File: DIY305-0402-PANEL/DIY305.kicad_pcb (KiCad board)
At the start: 2 copper layers, 49.8 x 26.6 mm, 152 parts, among them J1 Conn_01x07, J2 Conn_01x07, J3 Conn_01x07, J4 Conn_01x07, J5 Conn_01x07, J6 Conn_01x07, J7 Conn_01x07, J8 Conn_01x07

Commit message: Added pannel
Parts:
- removed D100, D101, D102, D103, D104, D105, D106, D107, D108, D109, D110, D111, D112, D113, D114, D115, D116, D117, D118, D119, D120, D121, D122, D123, D124, D125, D126, D127, D128, D129, D130, D131, D132, D133, D134, D135, D136, D137, D138, D139, D140, D141, D142, D143, D144, D37, D38, D39, D40, D41, D42, D43, D44, D45, D46, D47, D48, D49, D50, D51, D52, D53, D54, D55, D56, D57, D58, D59, D60, D61, D62, D63, D64, D65, D66, D67, D68, D69, D70, D71, D72, D73, D74, D75, D76, D77, D78, D79, D80, D81, D82, D83, D84, D85, D86, D87, D88, D89, D90, D91, D92, D93, D94, D95, D96, D97, D98, D99: LED, LED_SMD:LED_0402_1005Metric
- removed J3, J4, J5, J6, J7, J8: Conn_01x07, Connector_PinHeader_2.54mm:PinHeader_1x07_P2.54mm_Vertical
- moved J1 14.8 mm to (28.7, 21.6)
- moved D1 9.41 mm to (22.4, 23.2)
- moved D10 9.41 mm to (23.6, 27.2)
- moved D11 9.41 mm to (23.6, 29.2)
- moved D12 9.41 mm to (23.6, 31.2)
- moved D13 9.41 mm to (23.6, 33.2)
- moved D14 9.41 mm to (23.6, 35.2)
- moved D15 9.41 mm to (24.9, 23.2)
- moved D16 9.41 mm to (24.9, 25.2)
- moved D17 9.41 mm to (24.9, 27.2)
- moved D18 9.41 mm to (24.9, 29.2)
- moved D19 9.41 mm to (24.9, 31.2)
- moved D2 9.41 mm to (22.4, 25.2)
- moved D20 9.41 mm to (24.9, 33.2)
- moved D21 9.41 mm to (24.9, 35.2)
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- renumbered D11 to D10, D12 to D11, D13 to D12, D14 to D13, D15 to D14, D16 to D15, D17 to D16, D18 to D17, D19 to D18, D20 to D19, D21 to D20, D22 to D21, D23 to D22, D24 to D23, D25 to D24, D26 to D25, D27 to D26, D28 to D27, D29 to D28, D30 to D29, D31 to D30, D32 to D31, D33 to D32, D34 to D33, D35 to D34, D36 to D35, D8 to D36, D9 to D8, D10 to D9
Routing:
- net C1: track 142.1 -> 19.1 mm, vias 32 -> 7
- net C5: track 104.9 -> 17.8 mm, vias 32 -> 7
- net C4: track 92.0 -> 20.5 mm, vias 28 -> 7
- net C3: track 90.5 -> 22.0 mm, vias 28 -> 7
- net C2: track 86.6 -> 20.3 mm, vias 28 -> 7
- net R7: track 36.1 -> 10.5 mm
- net DP: track 25.7 -> 1.60 mm
- net R3: track 30.3 -> 6.53 mm
- net R1: track 30.0 -> 6.29 mm
- net R5: track 31.7 -> 8.39 mm
- net R4: track 29.5 -> 6.30 mm
- net R6: track 29.6 -> 7.96 mm
- net R2: track 26.1 -> 7.53 mm
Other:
- board size 49.8 x 26.6 mm -> 9.8 x 18.5 mm
- board text added: "Ru-Pirie"

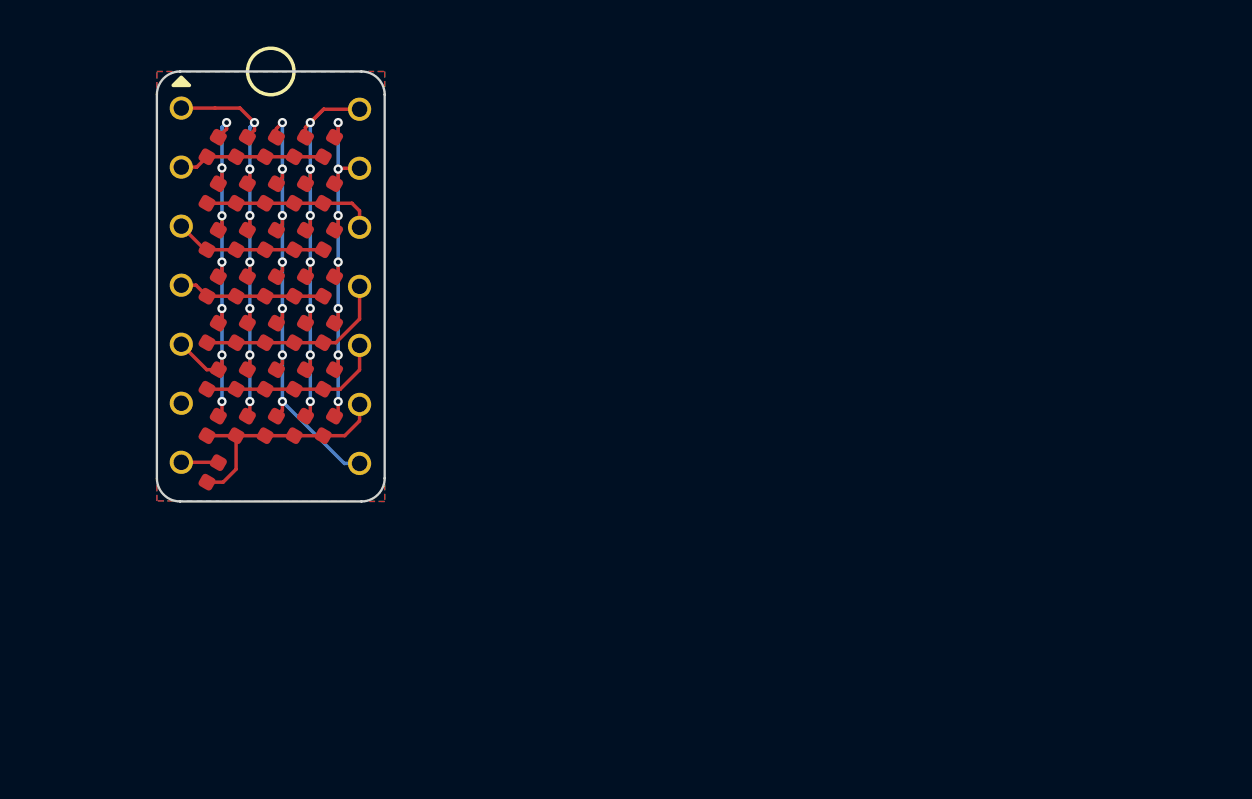
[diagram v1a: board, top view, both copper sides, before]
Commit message: generated panel and production files
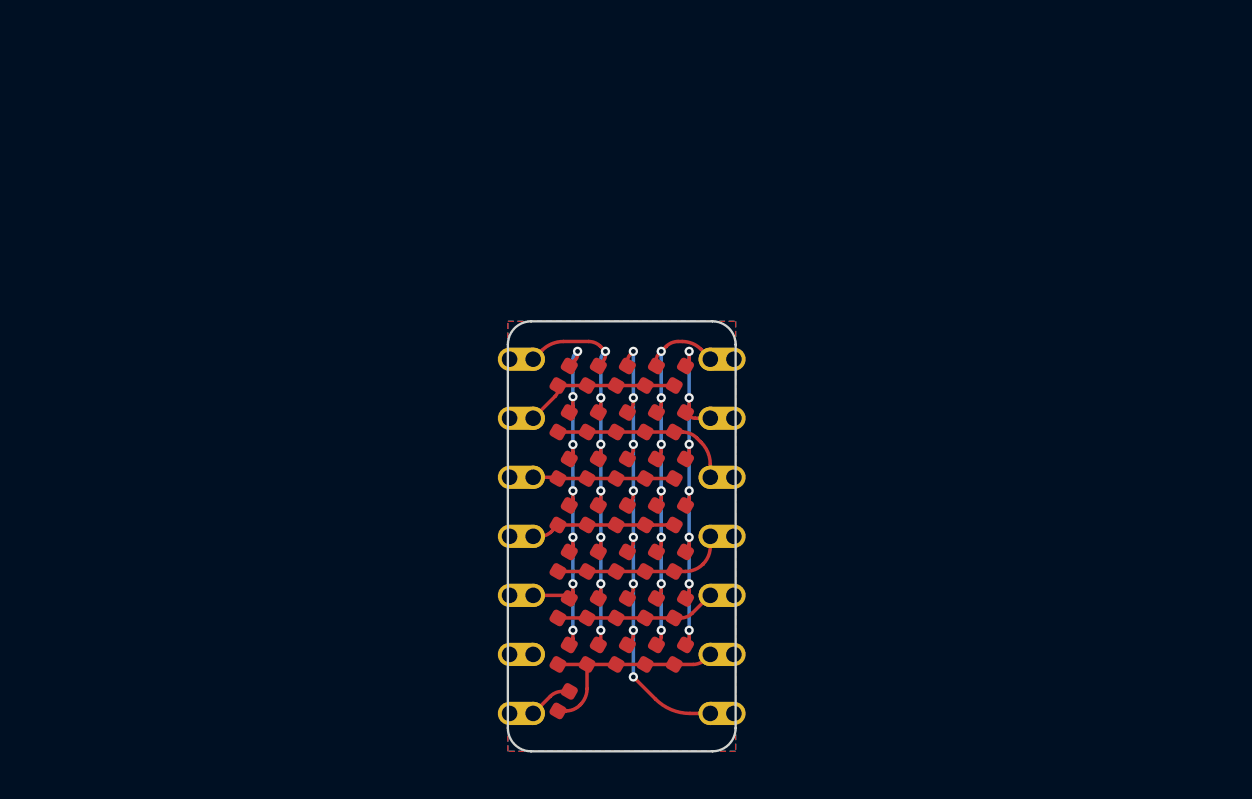
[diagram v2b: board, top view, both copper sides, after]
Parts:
- removed J1, J2: Conn_01x07, Connector_PinHeader_2.54mm:PinHeader_1x07_P2.54mm_Vertical
- added J3: Conn_01x14, Connector_PinHeader_1.00mm:PinHeader_1x14_P1.00mm_Vertical, F.Cu at (36.2, 32.4)
- moved D1 18.0 mm to (37.5, 33.1)
- moved D10 18.0 mm to (38.8, 37.1)
- moved D11 18.0 mm to (38.8, 39.1)
- moved D12 18.0 mm to (38.8, 41.1)
- moved D13 18.0 mm to (38.8, 43.1)
- moved D14 18.0 mm to (38.8, 45.1)
- moved D15 18.0 mm to (40.0, 33.1)
- moved D16 18.0 mm to (40.0, 35.1)
- moved D17 18.0 mm to (40.0, 37.1)
- moved D18 18.0 mm to (40.0, 39.1)
- moved D19 18.0 mm to (40.0, 41.1)
- moved D2 18.0 mm to (37.5, 35.1)
- moved D20 18.0 mm to (40.0, 43.1)
- moved D21 18.0 mm to (40.0, 45.1)
- moved D22 18.0 mm to (41.2, 33.1)
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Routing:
- net C4: track 20.5 -> 19.4 mm
- net R6: track 7.96 -> 6.92 mm
- net R7: track 10.5 -> 9.53 mm
- net C3: track 22.0 -> 22.9 mm, vias 7 -> 8
- net R5: track 8.39 -> 7.59 mm
- net C1: track 19.1 -> 18.6 mm
- net R1: track 6.29 -> 6.83 mm
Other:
- board text added: "DIY-305 Designed by Ru-Pirie and Envious.Design"
- board text removed: "Ru-Pirie"
